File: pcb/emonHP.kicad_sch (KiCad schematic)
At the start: 62 parts, among them CN1 CONN_03SCREW, CN3 Screw_Terminal_01x02, CN4 CONN_03SCREW, CN5 Screw_Terminal_01x02, J1 CONN_04PTH, J2 CONN_04PTH, J3 USB_C_Receptacle_USB2.0, J4 Conn_ARM_JTAG_SWD_10, J5 Conn_02x20_Odd_Even, SW1 SW_Push, SW2 SW_Push, U10 SN74LVC1T45DRL, U2 ATSAMD21G15B-A, U3 AP2112K-3.3, U4 RFM69CW, U9 USBLC6-2P6

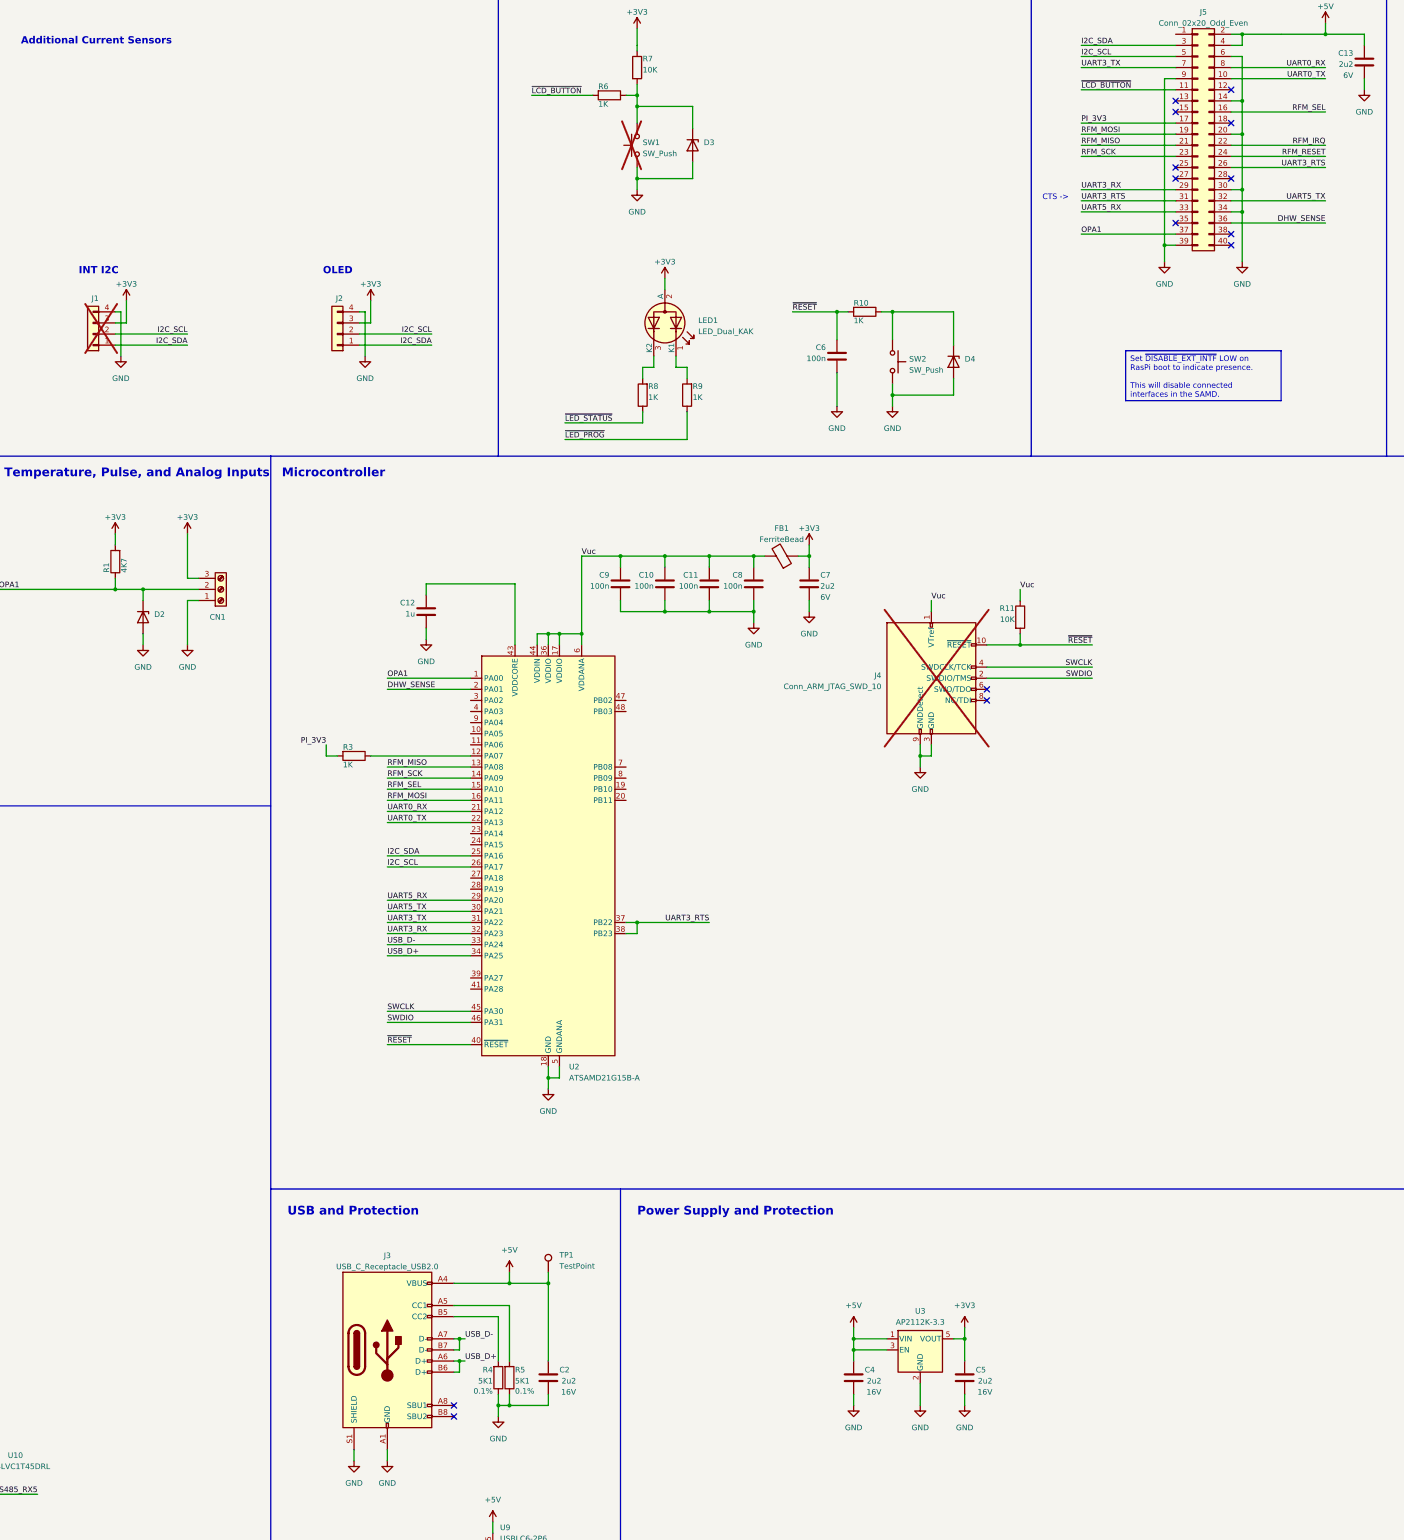
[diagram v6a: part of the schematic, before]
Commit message: Move SAMD below, reroute
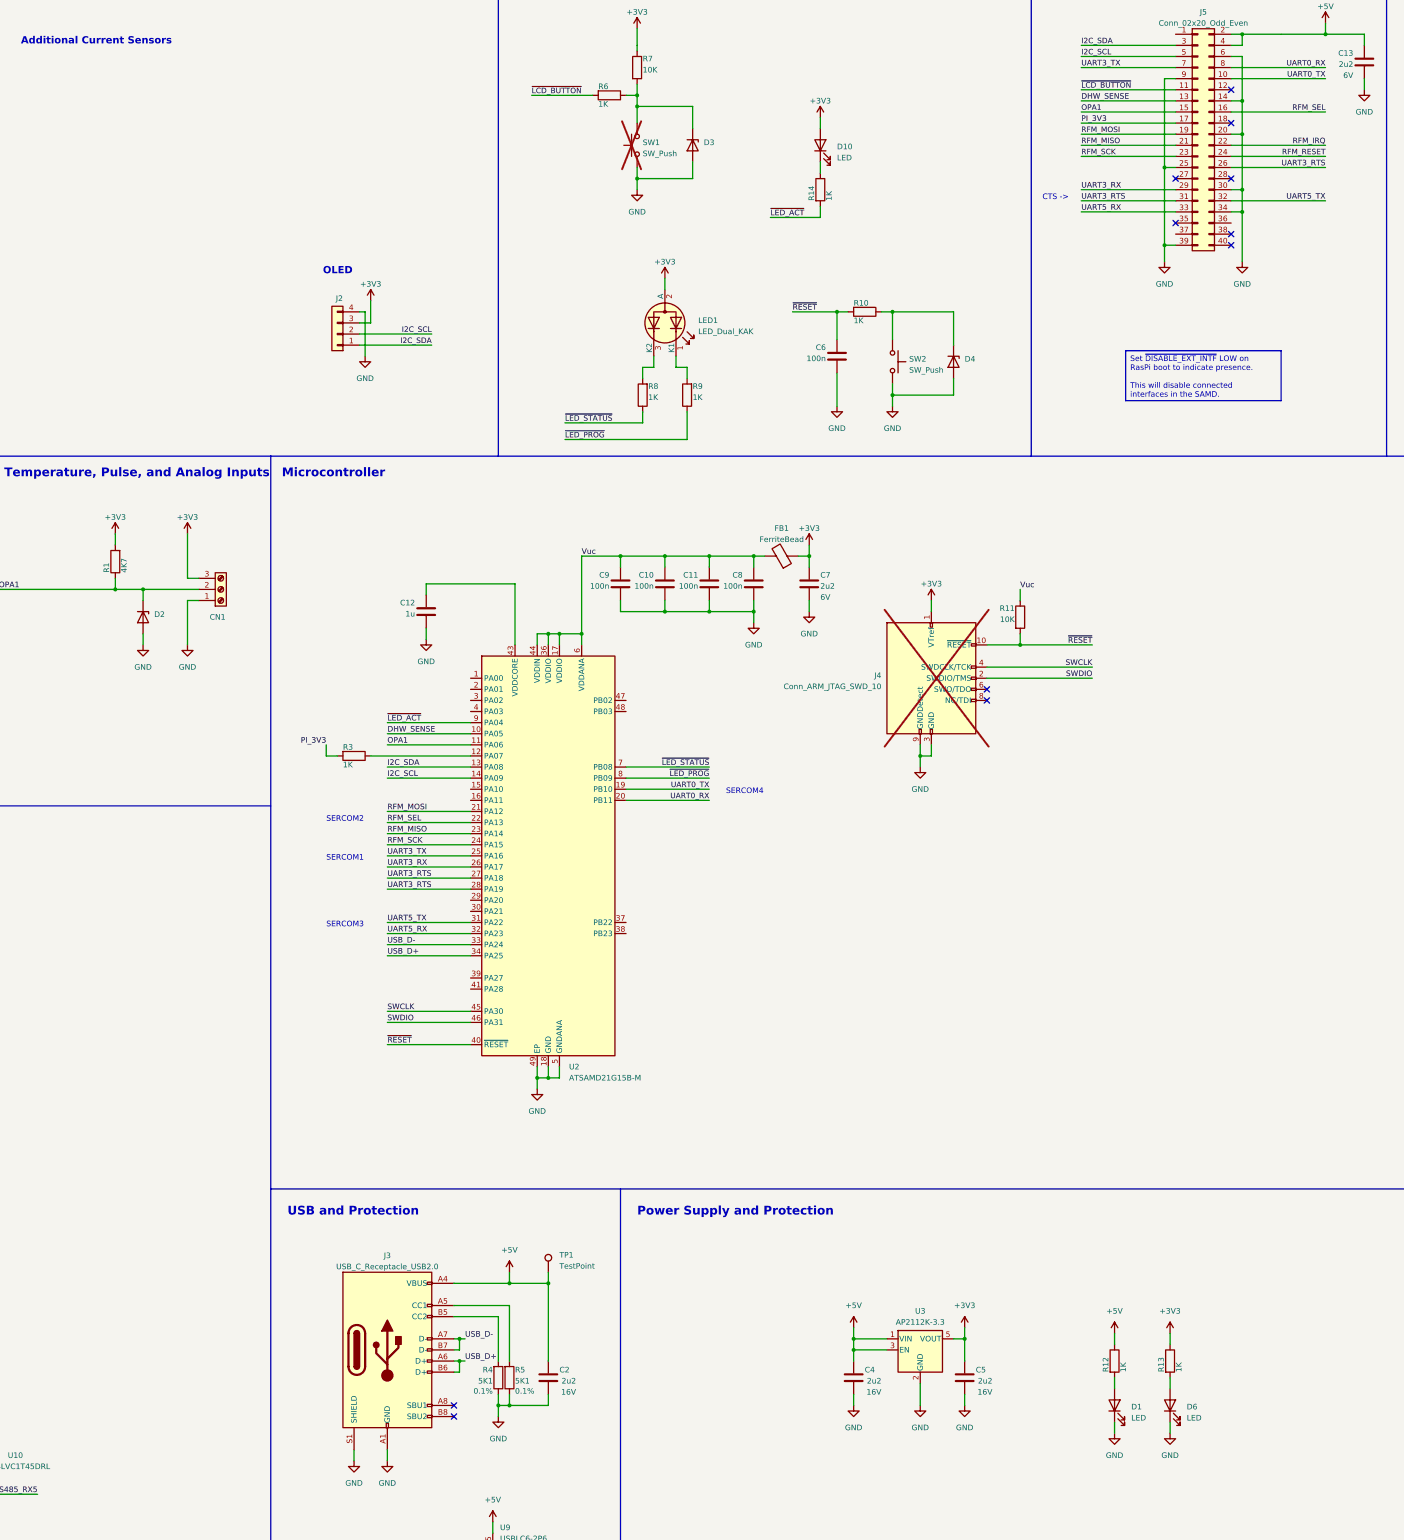
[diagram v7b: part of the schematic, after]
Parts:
- removed J1: CONN_04PTH, Connector_PinSocket_2.54mm:PinSocket_1x04_P2.54mm_Vertical, symbol Connector_Generic:Conn_01x04
- removed U2: ATSAMD21G15B-A, Package_QFP:TQFP-48_7x7mm_P0.5mm, symbol MCU_Microchip_SAMD:ATSAMD21G15B-A
- added D1, D10, D6: LED, LED_SMD:LED_0603_1608Metric, symbol Device:LED
- added R12, R13, R14: 1K, Resistor_SMD:R_0402_1005Metric, symbol Device:R
- added U2: ATSAMD21G15B-M, Package_DFN_QFN:QFN-48-1EP_7x7mm_P0.5mm_EP5.15x5.15mm, symbol MCU_Microchip_SAMD:ATSAMD21G15B-M
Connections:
- net +3V3: now also J4.1 (VTref), D10.2 (A), R13.1
- net +5V: now also R12.1
- net DHW_SENSE: now also J5.13 (Pin_13), U2.10 (PA05); no longer J5.36 (Pin_36)
- net GND: now also J5.25 (Pin_25), D1.1 (K), D6.1 (K), U2.18 (GND), U2.35 (GND), U2.42 (GND), U2.49 (EP), U2.5 (GNDANA)
- net I2C_SCL: now also U2.14 (PA09)
- net I2C_SDA: now also U2.13 (PA08)
- net OPA1: now also J5.15 (Pin_15), U2.11 (PA06); no longer J5.37 (Pin_37)
- net RFM_MISO: now also U2.23 (PA14)
- net RFM_MOSI: now also U2.21 (PA12)
- net RFM_SCK: now also U2.24 (PA15)
- net RFM_SEL: now also U2.22 (PA13)
- net SWCLK: now also U2.45 (PA30)
- net SWDIO: now also U2.46 (PA31)
- net UART0_RX: now also U2.20 (PB11)
- net UART0_TX: now also U2.19 (PB10)
- net UART3_RTS: now also U2.27 (PA18), U2.28 (PA19)
- net UART3_RX: now also U2.26 (PA17)
- net UART3_TX: now also U2.25 (PA16)
- net UART5_RX: now also U2.32 (PA23)
- net UART5_TX: now also U2.31 (PA22)
- net USB_D+: now also U2.34 (PA25)
- net USB_D-: now also U2.33 (PA24)
- net Vuc: now also U2.17 (VDDIO), U2.36 (VDDIO), U2.44 (VDDIN), U2.6 (VDDANA); no longer J4.1 (VTref)
- net ~{LED_PROG}: now also U2.8 (PB09)
- net ~{LED_STATUS}: now also U2.7 (PB08)
- net ~{RESET}: now also U2.40 (~{RESET})
- net at R3.1: now also U2.12 (PA07)
- net at C12.1: now also U2.43 (VDDCORE)
- new net: D6.2 (A), R13.2
- new net: D10.1 (K), R14.1
- new net: D1.2 (A), R12.2
- new net ~{LED_ACT}: R14.2, U2.9 (PA04)
- no-connect marks 18 -> 15
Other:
- note added: "SERCOM1"
- note added: "SERCOM2"
- note added: "SERCOM3"
- note added: "SERCOM4"
- note removed: "INT I2C"

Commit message: Swap 1Wire and AC sense
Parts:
- removed JP1: Jumper_2_Open, Jumper:SolderJumper-2_P1.3mm_Open_TrianglePad1.0x1.5mm, symbol Jumper:Jumper_2_Open
- removed R3: 1K, Resistor_SMD:R_0402_1005Metric, symbol Device:R
- removed TP7, TP8: TestPoint, TestPoint:TestPoint_Pad_D1.0mm, symbol Connector:TestPoint
- added R15, R16: 1K, Resistor_SMD:R_0402_1005Metric, symbol Device:R
- added TP2: TestPoint, TestPoint:TestPoint_Pad_D1.0mm, symbol Connector:TestPoint
- C10, C11, C15, C6, C7, C8, C9: LCSC (none) -> C1525
- C13, C14, C2, C4, C5: LCSC (none) -> C23630
- D1, D10, D6: LCSC (none) -> C2286
- J3: LCSC (none) -> C27636760; Note (none) -> LCSC is off-brand clone
- R1, R4, R5: LCSC (none) -> C25905
- R10, R12, R13, R14, R6, R8, R9: LCSC (none) -> C11702
- R17: value 47K -> 100K; LCSC (none) -> C25741
- R18, R19: value 4K7 -> 5K1; LCSC (none) -> C25905
- U10: LCSC (none) -> C352970
- U2: LCSC (none) -> C1341309
- U3: LCSC (none) -> C51118
- U9: LCSC (none) -> C15999
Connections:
- net +3V3: now also TP2.1
- net DHW_SENSE: now also J5.15 (Pin_15), U2.11 (PA06); no longer J5.13 (Pin_13), U2.10 (PA05)
- net GND: now also U2.39 (PA27), U2.41 (PA28)
- net MBUS_EN: now also U2.29 (PA20)
- net OPA1: now also J5.13 (Pin_13), U2.10 (PA05); no longer J5.15 (Pin_15), U2.11 (PA06)
- net UART3_RTS: now also R16.2; no longer U2.27 (PA18), U2.28 (PA19)
- net UART3_TX: now also R15.2; no longer U2.25 (PA16)
- net ~{PI_PRESENT}: now reaches U2.12 (PA07)
- net ~{PI_PRESENT}: now also J5.18 (Pin_18)
- net PI_3V3: no longer names the net of J5.17 (Pin_17)
- new net UART3_RTS_uc: R16.1, U2.27 (PA18), U2.28 (PA19)
- new net UART3_TX_uc: R15.1, U2.25 (PA16)
- no-connect marks 15 -> 25
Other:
- note added: "External Interfaces"
- note added: "I^{2}C header"
- note added: "SERCOM0"
- note removed: "Additional Current Sensors"
- note removed: "CT Current Sensors"
- note removed: "EEPROM"
- note removed: "Optional Headers"
- note removed: "Temperature, Pulse, and Analog Inputs"
- moved on the sheet: CN1, CN3, CN4, CN5, D2, J2, R1, R18, R19, TP5, U10
